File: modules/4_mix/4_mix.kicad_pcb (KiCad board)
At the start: 2 copper layers, 61 x 68.6 mm, 38 parts, among them U1 LM358, U2 LM358, U3 LM358

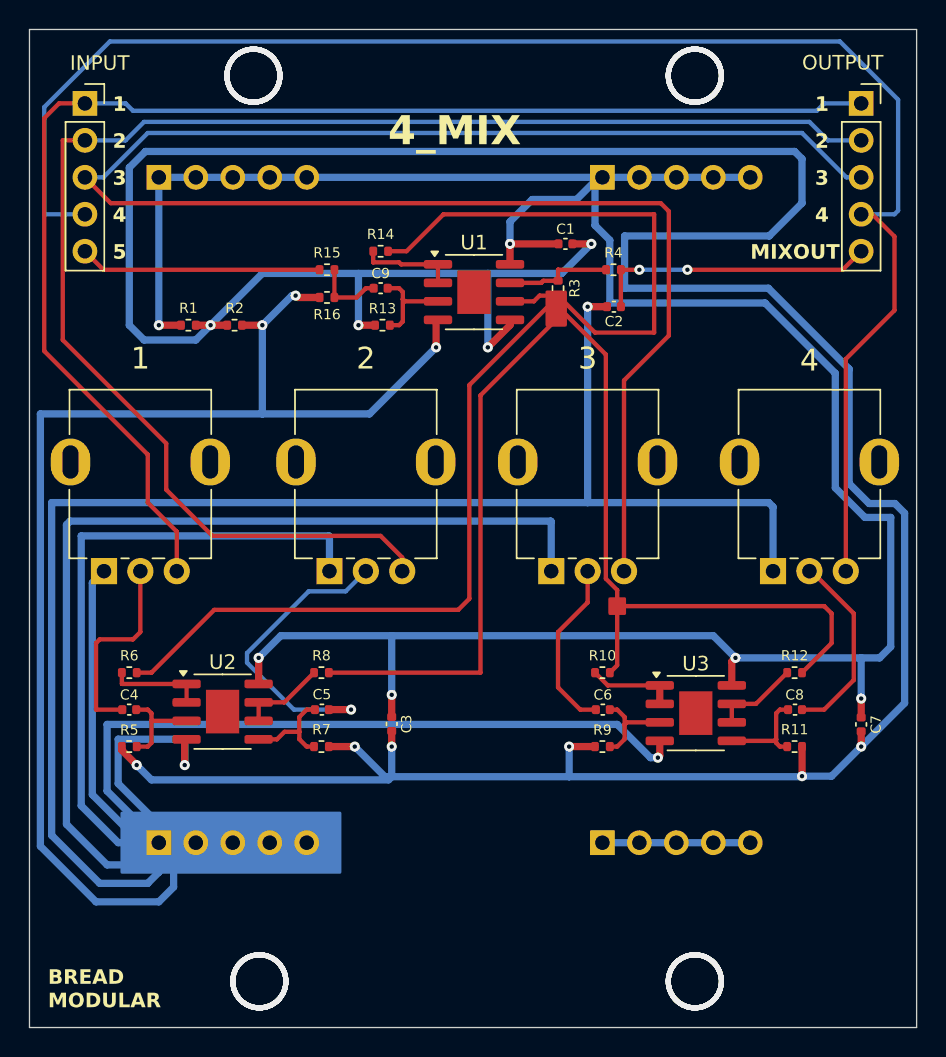
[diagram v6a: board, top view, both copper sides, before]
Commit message: Use TL072 the current version has some pops and cracks LM358 could be the issue. So, we are trying TL072
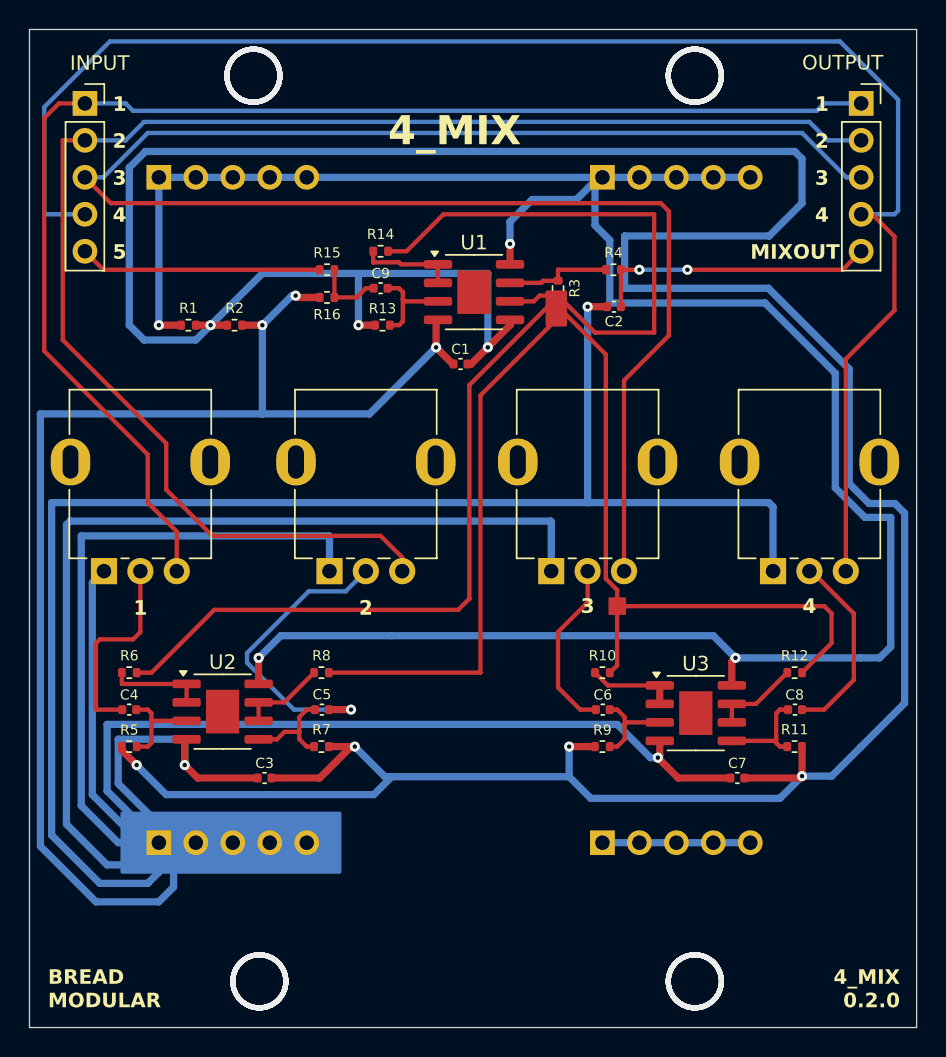
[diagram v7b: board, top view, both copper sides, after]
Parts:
- 1, 2, 3, 4: footprint BreadModular_OPT1:Potentiometer_RV09 -> BreadModular_Pots:Potentiometer_RV09
- U1, U2, U3: value LM358 -> TL072
- moved C1 11.0 mm to (76.6, 63.6)
- moved C3 9.49 mm to (63.1, 92.1), turned to 0 degrees
- moved C7 9.27 mm to (95.6, 92.1), turned to 0 degrees
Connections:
- C1 pad 1: +5V -> GND
- C3 pad 1: +5V -> GND
- C7 pad 1: +5V -> GND
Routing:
- net +5V: track 172.9 -> 159.8 mm, vias 6 -> 4
- net GND: track 398.6 -> 411.2 mm
- net 2.5V: track 243.8 -> 244.9 mm, vias 10 -> 7
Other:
- board text added: "4_MIX 0.2.0"

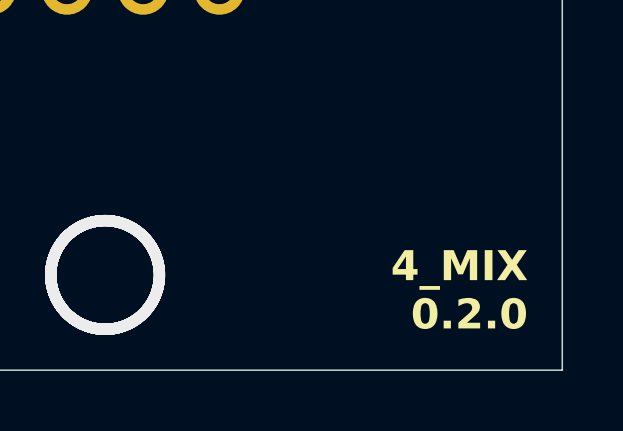
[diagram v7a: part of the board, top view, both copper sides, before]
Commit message: Use MCP6002 in the 4_mix. This provides more headroom due to it's rail-2-rail output.
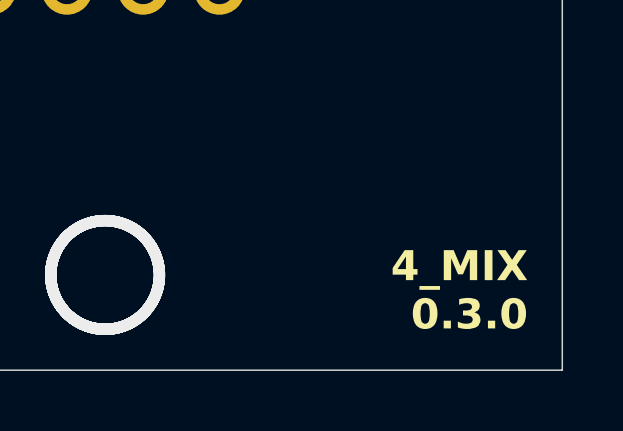
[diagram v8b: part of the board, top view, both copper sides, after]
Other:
- board text added: "4_MIX 0.3.0"
- board text removed: "4_MIX 0.2.0"
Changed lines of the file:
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@@
 		)
 	)
-	(gr_text "4_MIX\n0.2.0"
+	(gr_text "4_MIX\n0.3.0"
 		(at 106.807 107.95 0)
 		(layer "F.SilkS")
